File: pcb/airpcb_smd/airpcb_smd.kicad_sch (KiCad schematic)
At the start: 29 parts, among them J1 SPI, J11 PSU, J2 DHT, J3 DC, J4 AB, J5 Conn_01x08, J6 Conn_01x08, J7 PWR, J8 WS2812, J9 5V3V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

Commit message: routing
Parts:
- removed D5: 1N4001, Diode_SMD:D_SMA, symbol Diode:1N4001
- removed J11: PSU, airpcb_smd:HW-108, symbol Connector_Generic:Conn_01x05
- removed J3: DC, Connector_PinSocket_2.54mm:PinSocket_1x02_P2.54mm_Vertical, symbol Connector_Generic:Conn_01x02
- removed J5, J6: Conn_01x08, Connector_PinSocket_2.54mm:PinSocket_1x08_P2.54mm_Vertical, symbol Connector_Generic:Conn_01x08
- removed J9: 5V3V, Connector_PinSocket_2.54mm:PinSocket_1x03_P2.54mm_Vertical, symbol Connector_Generic:Conn_01x03
- removed R8: 100, Resistor_SMD:R_0805_2012Metric, symbol Device:R
- removed U3: WeMos_D1_mini, Module:WEMOS_D1_mini_light, symbol MCU_Module:WeMos_D1_mini
- removed U4: ESP-12E, RF_Module:ESP-12E, symbol RF_Module:ESP-12E
- added U3: NodeMCU_ESP-12E, nodemcu:NodeMCU_ESP-12E_WithMountingHoles, symbol MCU_Module_esp:NodeMCU_ESP-12E
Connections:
- net 3V3: now also J1.2 (Pin_2), J2.3 (Pin_3), U3.11 (+3V3), U3.16 (+3V3), U3.25 (+3V3); no longer J1.1 (Pin_1), J2.1 (Pin_1)
- net A0: now also U3.2 (ADC)
- net D0: now also U3.30 (D0/IO16)
- net D3: now also U3.27 (D3/IO0)
- net D4: now also U3.26 (D4/TX1/IO2)
- net D5: now also U3.23 (D5/SCLK/IO14)
- net D6: now also U3.22 (D6/MISO/IO12)
- net D7: now also U3.21 (D7/RX2/MOSI/IO13)
- net D8: now also U3.20 (D8/TX2/SPI_SS/IO15)
- net ESP_RX: now also U3.19 (D9/RX0/IO3)
- net ESP_TX: now also U3.18 (D10/TX0/IO1)
- net GND: now also J1.1 (Pin_1), J2.1 (Pin_1), J7.1 (Pin_1), J8.1 (Pin_1), U3.10 (GND), U3.14 (GND), U3.17 (GND), U3.24 (GND); no longer J1.2 (Pin_2), J2.4 (Pin_4), J7.3 (Pin_3), J8.3 (Pin_3)
- net RST: now also U3.13 (~{RST})
- net SCL: now also U3.28 (D2/I2C_SDA/IO4)
- net SDA: now also U3.29 (D1/I2C_SCL/IO5)
- net VCC: now also J7.3 (Pin_3), J8.3 (Pin_3), U3.15 (VIN); no longer J7.1 (Pin_1), J8.1 (Pin_1)
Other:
- note added: "NodeMCU ESP 12E"
- note removed: "ESP12E Module"
- note removed: "Expansion headers for Wemos D1 mini"
- note removed: "Wemos D1 mini"
- moved on the sheet: D1, D2, D3, D4, J1, J2, J4, J7, J8, Q1, Q2, R1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

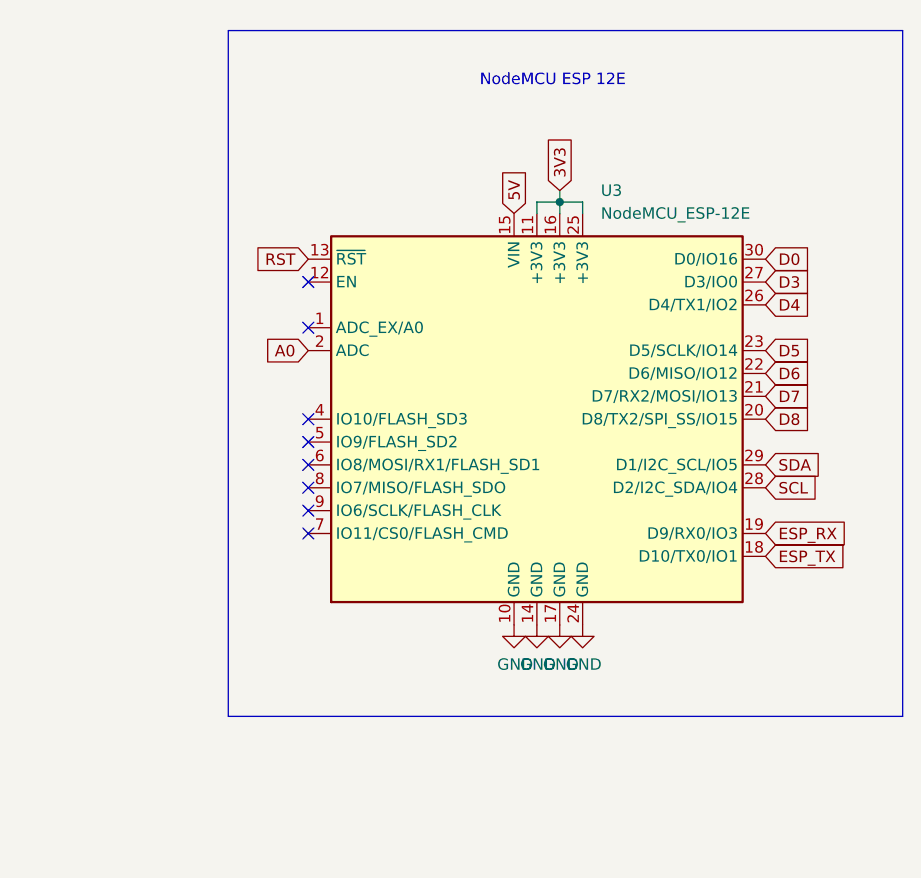
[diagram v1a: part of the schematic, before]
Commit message: added esp32 in schematic
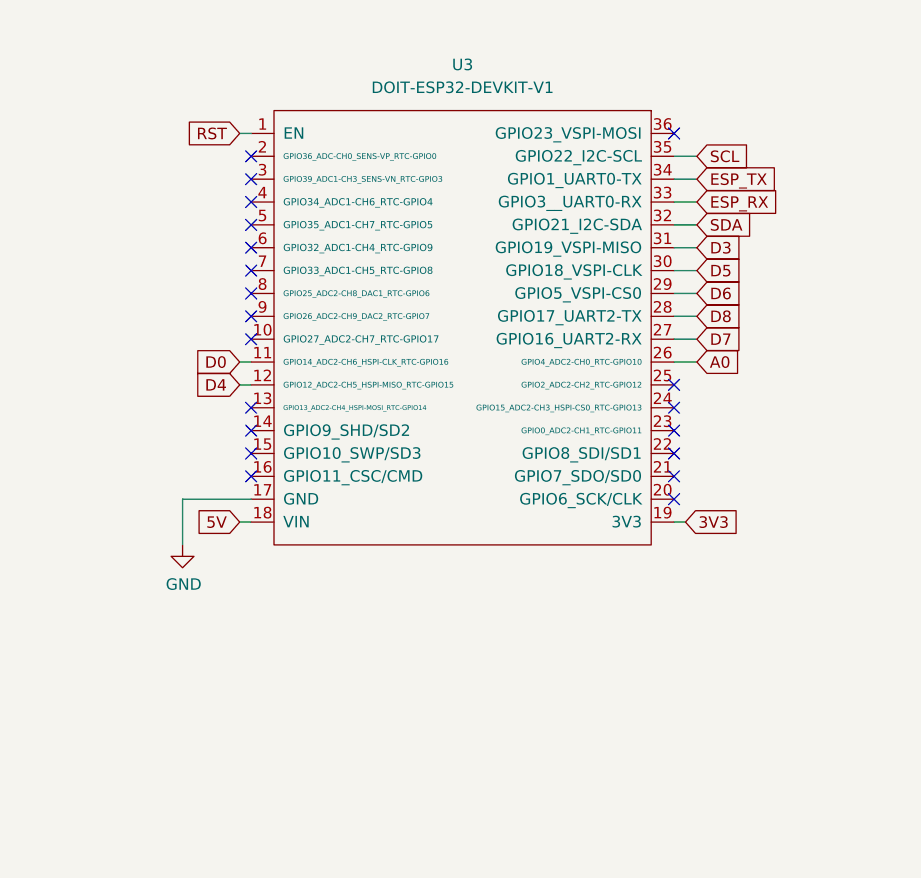
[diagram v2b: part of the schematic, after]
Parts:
- removed U3: NodeMCU_ESP-12E, nodemcu:NodeMCU_ESP-12E_WithMountingHoles, symbol MCU_Module_esp:NodeMCU_ESP-12E
- added U3: DOIT-ESP32-DEVKIT-V1, symbol doit-esp32-devkit-v1:DOIT-ESP32-DEVKIT-V1
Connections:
- net 3V3: now also U3.19 (3V3)
- net A0: now also U3.26 (GPIO4_ADC2-CH0_RTC-GPIO10)
- net D0: now also U3.11 (GPIO14_ADC2-CH6_HSPI-CLK_RTC-GPIO16)
- net D3: now also U3.31 (GPIO19_VSPI-MISO)
- net D4: now also U3.12 (GPIO12_ADC2-CH5_HSPI-MISO_RTC-GPIO15)
- net D5: now also U3.30 (GPIO18_VSPI-CLK)
- net D6: now also U3.29 (GPIO5_VSPI-CS0)
- net D7: now also U3.27 (GPIO16_UART2-RX)
- net D8: now also U3.28 (GPIO17_UART2-TX)
- net ESP_RX: now also U3.33 (GPIO3__UART0-RX)
- net ESP_TX: now also U3.34 (GPIO1_UART0-TX)
- net GND: now also U3.17 (GND)
- net RST: now also U3.1 (EN)
- net SCL: now also U3.35 (GPIO22_I2C-SCL)
- net SDA: now also U3.32 (GPIO21_I2C-SDA)
- net VCC: now also U3.18 (VIN)
- no-connect marks 9 -> 21
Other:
- note removed: "NodeMCU ESP 12E"

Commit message: schematic done
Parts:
- removed U3: DOIT-ESP32-DEVKIT-V1, symbol doit-esp32-devkit-v1:DOIT-ESP32-DEVKIT-V1
- added D5: 1N4001, Diode_SMD:D_SMA, symbol Diode:1N4001
- added J11: PSU, Connector_PinSocket_2.54mm:PinSocket_1x05_P2.54mm_Vertical, symbol Connector_Generic:Conn_01x05
- added J3: DC, Connector_PinSocket_2.54mm:PinSocket_1x02_P2.54mm_Vertical, symbol Connector_Generic:Conn_01x02
- added J9: 5V3V, Connector_PinSocket_2.54mm:PinSocket_1x03_P2.54mm_Vertical, symbol Connector_Generic:Conn_01x03
- added R8: 100, Resistor_SMD:R_0805_2012Metric, symbol Device:R
- added U3: ESP32-DEVKIT-V1, symbol ESP32-DEVKIT-V1:ESP32-DEVKIT-V1
- J1: value SPI -> I2C
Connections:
- net 3V3: now also J9.3 (Pin_3), U3.1 (3V3)
- net A: now also R8.2
- net B: now also J11.4 (Pin_4)
- net D4: now also U3.5 (D4)
- net GND: now also J11.1 (Pin_1), U3.2 (GND), U3.29 (GND)
- net SCL: now also U3.14 (D22)
- net SDA: now also U3.11 (D21)
- net VCC: now also J9.1 (Pin_1), U3.30 (VIN)
- net D3 renamed D2
- net D2: now also U3.4 (D2)
- net D7 renamed D12
- net D12: now also U3.27 (D12)
- net D8 renamed D13
- net D13: now also U3.28 (D13)
- new net: D5.2 (A), R8.1
- new net: J11.3 (Pin_3), J3.2 (Pin_2)
- new net: D5.1 (K), J3.1 (Pin_1)
- new net PSU_OUT: J11.2 (Pin_2), J9.2 (Pin_2)
- no-connect marks 21 -> 22

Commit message: pcb wip
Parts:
- added H1, H2, H3, H4: MountingHole, MountingHole:MountingHole_2.2mm_M2_DIN965_Pad, symbol Mechanical:MountingHole
- U3: footprint (none) -> airpcb_smd:MODULE_ESP32_DEVKIT_V1
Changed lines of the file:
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@@
     (property "Reference" "U3" (id 0) (at 228.6 30.48 0))
     (property "Value" "ESP32-DEVKIT-V1" (id 1) (at 228.6 33.02 0))
-    (property "Footprint" "" (id 2) (at 228.6 63.5 0)
+    (property "Footprint" "airpcb_smd:MODULE_ESP32_DEVKIT_V1" (id 2) (at 228.6 63.5 0)
       (effects (font (size 1.27 1.27)) (justify left bottom) hide)
     )
@@
     (pin "9")
   )
+  (symbol (lib_id "Mechanical:MountingHole") (at 158.75 179.07 0) (unit 1)
+    (in_bom yes) (on_board yes) (fields_autoplaced)
+    (property "Reference" "H3" (id 0) (at 161.29 177.7999 0)
+      (effects (font (size 1.27 1.27)) (justify left))
+    )
+    (property "Value" "MountingHole" (id 1) (at 161.29 180.3399 0)
+      (effects (font (size 1.27 1.27)) (justify left))
+    )
+    (property "Footprint" "MountingHole:MountingHole_2.2mm_M2_DIN965_Pad" (id 2) (at 158.75 179.07 0)
+      (effects (font (size 1.27 1.27)) hide)
+    )
+    (property "Datasheet" "~" (id 3) (at 158.75 179.07 0)
+      (effects (font (size 1.27 1.27)) hide)
+    )
+  )
   (symbol (lib_id "Device:R") (at 119.38 67.31 270) (unit 1)
     (in_bom yes) (on_board yes)
@@
     (pin "2")
   )
+  (symbol (lib_id "Mechanical:MountingHole") (at 158.75 171.45 0) (unit 1)
+    (in_bom yes) (on_board yes) (fields_autoplaced)
+    (property "Reference" "H2" (id 0) (at 161.29 170.1799 0)
+      (effects (font (size 1.27 1.27)) (justify left))
+    )
+    (property "Value" "MountingHole" (id 1) (at 161.29 172.7199 0)
+      (effects (font (size 1.27 1.27)) (justify left))
+    )
+    (property "Footprint" "MountingHole:MountingHole_2.2mm_M2_DIN965_Pad" (id 2) (at 158.75 171.45 0)
+      (effects (font (size 1.27 1.27)) hide)
+    )
+    (property "Datasheet" "~" (id 3) (at 158.75 171.45 0)
+      (effects (font (size 1.27 1.27)) hide)
+    )
+  )
+  (symbol (lib_id "Mechanical:MountingHole") (at 158.75 186.69 0) (unit 1)
+    (in_bom yes) (on_board yes) (fields_autoplaced)
+    (property "Reference" "H4" (id 0) (at 161.29 185.4199 0)
+      (effects (font (size 1.27 1.27)) (justify left))
+    )
+    (property "Value" "MountingHole" (id 1) (at 161.29 187.9599 0)
+      (effects (font (size 1.27 1.27)) (justify left))
+    )
+    (property "Footprint" "MountingHole:MountingHole_2.2mm_M2_DIN965_Pad" (id 2) (at 158.75 186.69 0)
+      (effects (font (size 1.27 1.27)) hide)
+    )
+    (property "Datasheet" "~" (id 3) (at 158.75 186.69 0)
+      (effects (font (size 1.27 1.27)) hide)
+    )
+  )
+  (symbol (lib_id "Mechanical:MountingHole") (at 158.75 163.83 0) (unit 1)
+    (in_bom yes) (on_board yes) (fields_autoplaced)
+    (property "Reference" "H1" (id 0) (at 161.29 162.5599 0)
+      (effects (font (size 1.27 1.27)) (justify left))
+    )
+    (property "Value" "MountingHole" (id 1) (at 161.29 165.0999 0)
+      (effects (font (size 1.27 1.27)) (justify left))
+    )
+    (property "Footprint" "MountingHole:MountingHole_2.2mm_M2_DIN965_Pad" (id 2) (at 158.75 163.83 0)
+      (effects (font (size 1.27 1.27)) hide)
+    )
+    (property "Datasheet" "~" (id 3) (at 158.75 163.83 0)
+      (effects (font (size 1.27 1.27)) hide)
+    )
+  )
   (symbol (lib_id "Connector_Generic:Conn_01x03") (at 129.54 48.26 0) (unit 1)
     (in_bom yes) (on_board yes)
@@
       (reference "D5") (unit 1) (value "1N4001") (footprint "Diode_SMD:D_SMA")
     )
+    (path "/4d8bdf70-7048-49da-a8fe-e0b852d93686"
+      (reference "H1") (unit 1) (value "MountingHole") (footprint "MountingHole:MountingHole_2.2mm_M2_DIN965_Pad")
+    )
+    (path "/307a2177-7b34-4d1a-ab45-4c19144d4af4"
+      (reference "H2") (unit 1) (value "MountingHole") (footprint "MountingHole:MountingHole_2.2mm_M2_DIN965_Pad")
+    )
+    (path "/27f7df19-e392-4c58-b260-98ddfc60d5e8"
+      (reference "H3") (unit 1) (value "MountingHole") (footprint "MountingHole:MountingHole_2.2mm_M2_DIN965_Pad")
+    )
+    (path "/32847d0e-fa87-4c59-b9d6-5fdb1a90d67e"
+      (reference "H4") (unit 1) (value "MountingHole") (footprint "MountingHole:MountingHole_2.2mm_M2_DIN965_Pad")
+    )
     (path "/00000000-0000-0000-0000-00005f5f93c3"
       (reference "J1") (unit 1) (value "I2C") (footprint "Connector_PinSocket_2.54mm:PinSocket_1x04_P2.54mm_Vertical")
@@
     )
     (path "/1f2f7032-ff76-4422-ad75-bc0b61f7e3ef"
-      (reference "U3") (unit 1) (value "ESP32-DEVKIT-V1") (footprint "")
-    )
-  )
+      (reference "U3") (unit 1) (value "ESP32-DEVKIT-V1") (footprint "airpcb_smd:MODULE_ESP32_DEVKIT_V1")
+    )
+  )
